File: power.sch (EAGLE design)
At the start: 12 parts, among them IC1 UC27775, J2 USB-MINIB-TH-VERTICAL-5PIN, U1 MCP73831, U2 Tiny85-20-SMT, X1 Micro USB

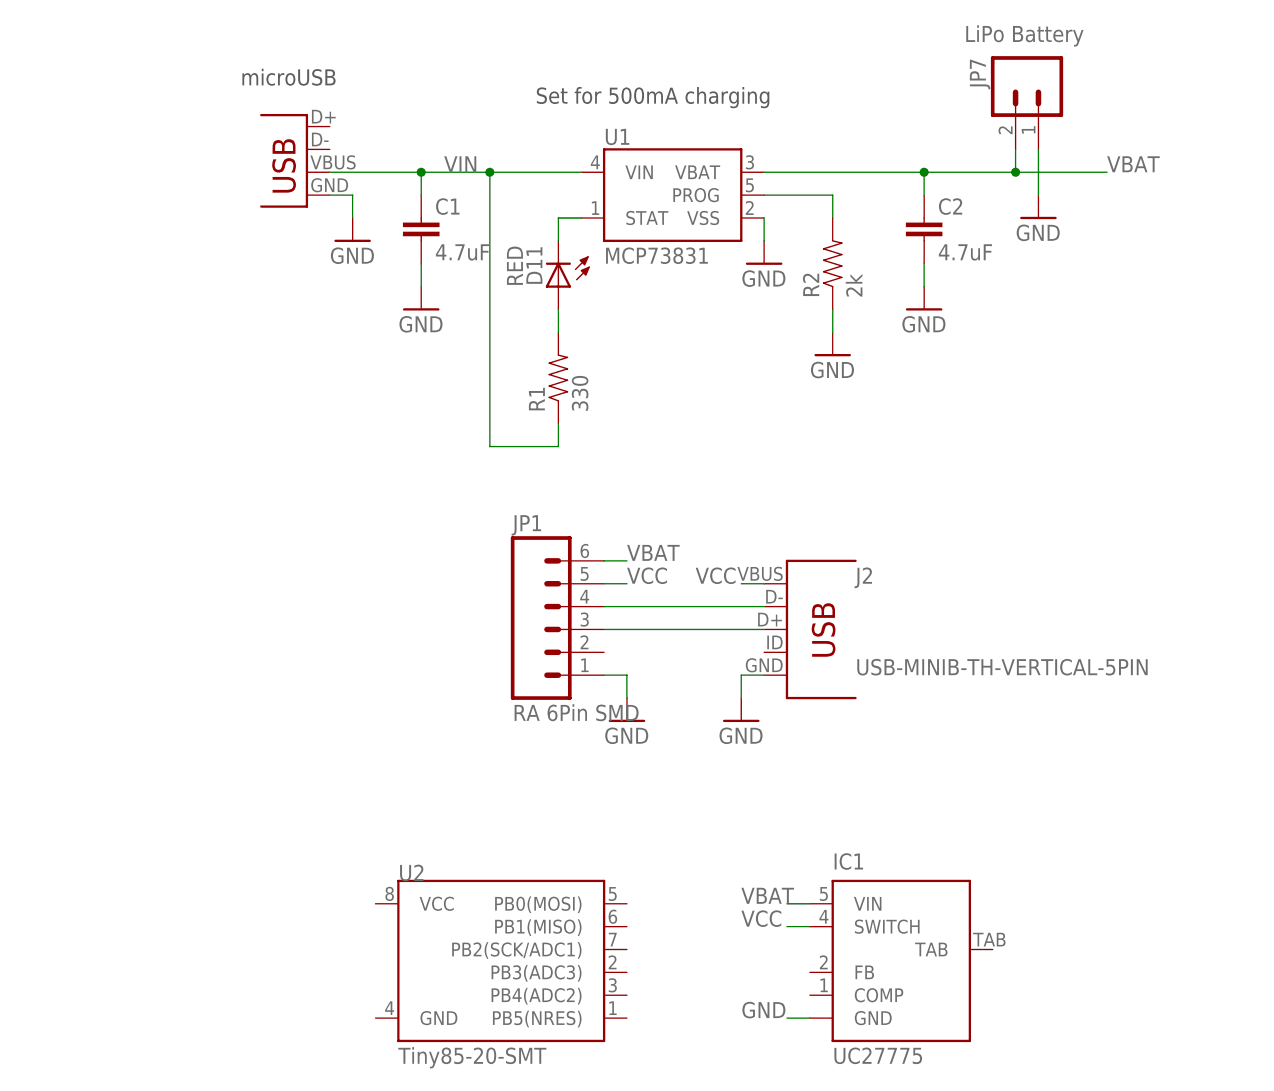
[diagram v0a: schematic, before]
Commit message: Added a switch and cleaned up the drawings
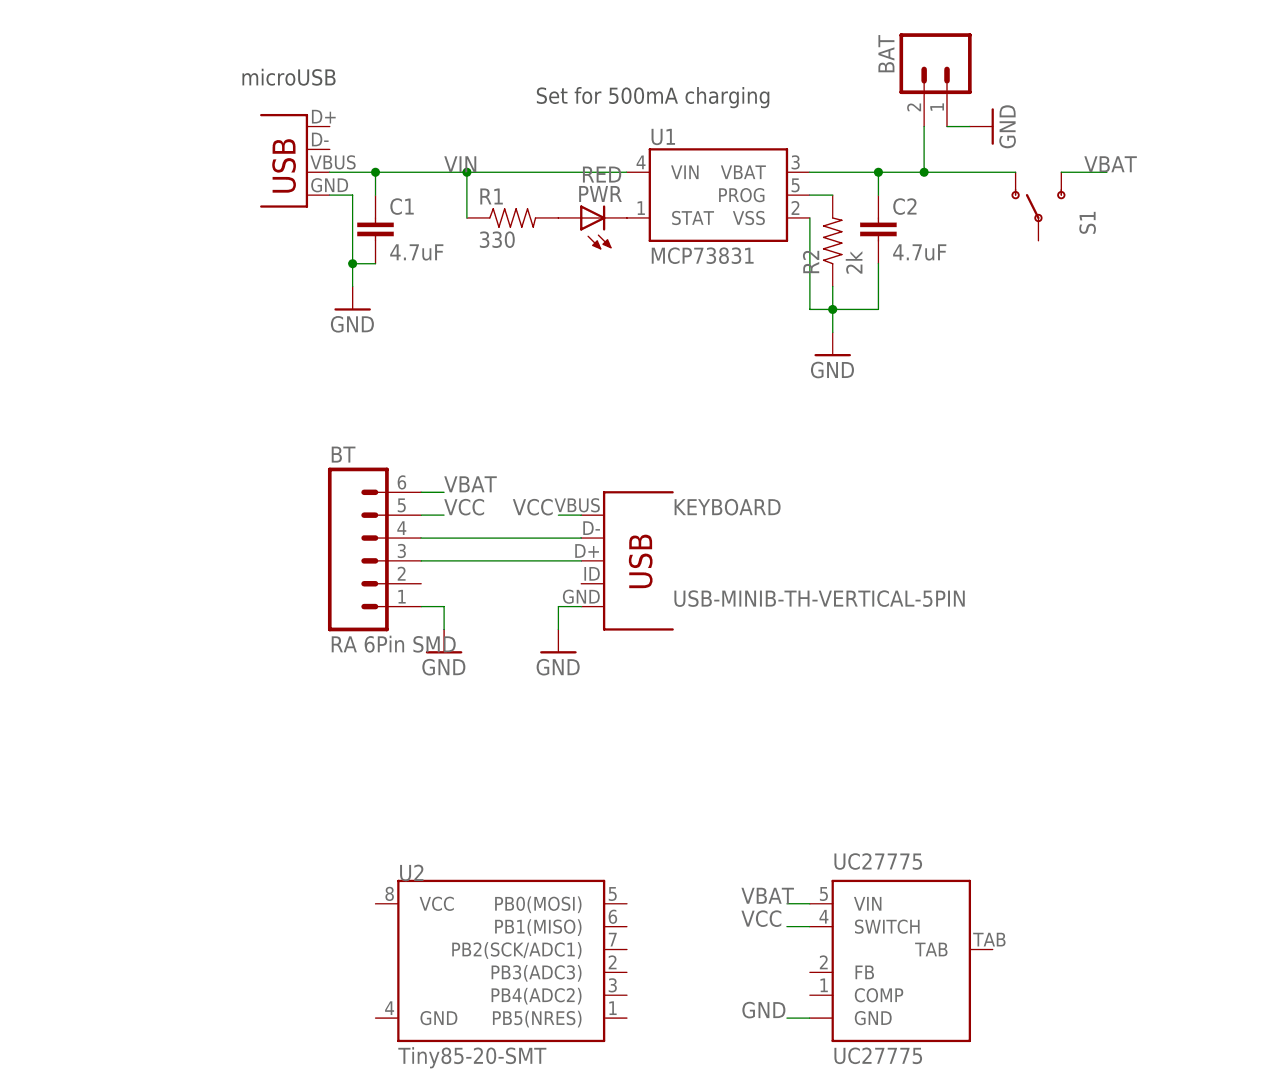
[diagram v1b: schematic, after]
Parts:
- removed D11: RED, SparkFun:LED0603
- removed J2: USB-MINIB-TH-VERTICAL-5PIN, mine:USB-MINIB-TH-VERTICAL-5PIN
- removed JP1: RA 6Pin SMD, mine:M06SMD-NOHOLES
- removed JP7: LiPo Battery, SparkFun:M02-JST-2MM-SMT
- added BAT: LiPo Battery, SparkFun:M02-JST-2MM-SMT
- added BT: RA 6Pin SMD, mine:M06SMD-NOHOLES
- added KEYBOARD: USB-MINIB-TH-VERTICAL-5PIN, mine:USB-MINIB-TH-VERTICAL-5PIN
- added PWR: RED, SparkFun:LED0603
- added S1: (no value), SparkFun-Electromechanical:SWITCH-SPDT-SMD-A
- renumbered IC1 to UC27775
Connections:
- new net VBAT2: BAT.2, C2.1, S1.O, U1.VBAT
- net GND: now also BAT.1, BT.1, KEYBOARD.GND; no longer J2.GND, JP1.1, JP7.1
- net N$12: now also PWR.A; no longer D11.A
- net N$2: now also BT.4, KEYBOARD.D-; no longer J2.D-, JP1.4
- net N$3: now also BT.3, KEYBOARD.D+; no longer J2.D+, JP1.3
- net STAT: now also PWR.C; no longer D11.C
- net VBAT: now also BT.6, S1.S; no longer C2.1, JP1.6, JP7.2, U1.VBAT
- net VCC: now also BT.5, KEYBOARD.VBUS; no longer J2.VBUS, JP1.5
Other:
- moved on the sheet: C1, C2, R1, R2, U1

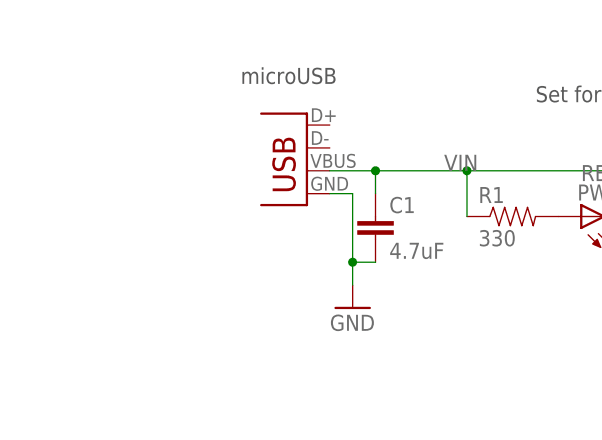
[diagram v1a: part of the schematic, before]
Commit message: Using mini usb instead of micro
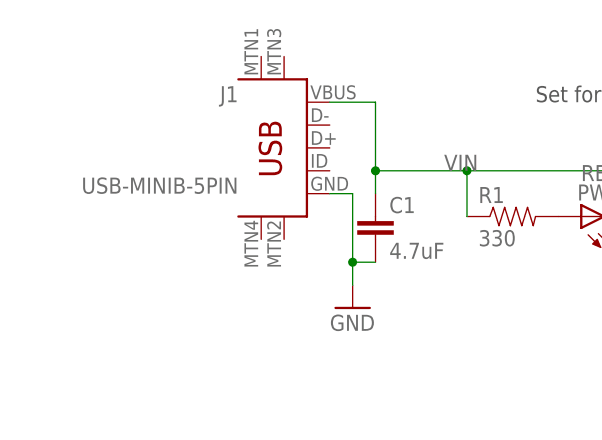
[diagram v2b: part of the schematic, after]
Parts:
- removed X1: Micro USB, SparkFun:USB-MICROB
- added J1: USB-MINIB-5PIN, SparkFun-Connectors:USB-MINIB-5PIN
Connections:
- net GND: now also J1.GND; no longer X1.GND
- net VIN: now also J1.VBUS; no longer X1.VBUS
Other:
- note removed: "microUSB"
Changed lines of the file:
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@@
 <?xml version="1.0" encoding="utf-8"?>
 <!DOCTYPE eagle SYSTEM "eagle.dtd">
-<eagle version="6.6.0">
+<eagle version="7.4.0">
 <drawing>
 <settings>
@@
 <part name="GND19" library="SparkFun" deviceset="GND" device=""/>
 <part name="BAT" library="SparkFun" deviceset="M02" device="-JST-2MM-SMT" value="LiPo Battery"/>
-<part name="X1" library="SparkFun" deviceset="USB" device="-MICROB" value="Micro USB"/>
 <part name="R2" library="SparkFun-Resistors" deviceset="0.22OHM-1/4W-1%(0805)" device="" value="2k"/>
 <part name="C1" library="SparkFun-Capacitors" deviceset="1.0UF-25V-+80/-20(0805)" device="&quot;" value="4.7uF"/>
@@
 <part name="KEYBOARD" library="mine" deviceset="USB-MINIB-TH-VERTICAL" device="-5PIN"/>
 <part name="S1" library="SparkFun-Electromechanical" deviceset="SWITCH-SPDT" device="-SMD-A"/>
+<part name="J1" library="SparkFun-Connectors" deviceset="USB-MINIB" device="-5PIN"/>
 </parts>
 <sheets>
@@
 <plain>
 <text x="167.64" y="142.24" size="1.778" layer="97">Set for 500mA charging</text>
-<text x="134.874" y="144.272" size="1.778" layer="97">microUSB</text>
 </plain>
 <instances>
@@
 <attribute name="NAME" x="207.518" y="149.86" size="1.778" layer="95" rot="MR270"/>
 </instance>
-<instance part="X1" gate="G$1" x="142.24" y="132.08" rot="MR0"/>
 <instance part="R2" gate="G$1" x="200.66" y="127" rot="R90"/>
 <instance part="C1" gate="G$1" x="149.86" y="127"/>
@@
 <instance part="KEYBOARD" gate="G$1" x="175.26" y="86.36"/>
 <instance part="S1" gate="1" x="223.52" y="129.54" rot="R90"/>
+<instance part="J1" gate="G$1" x="142.24" y="132.08" rot="MR0"/>
 </instances>
 <busses>
@@
 <wire x1="147.32" y1="132.08" x2="147.32" y2="124.46" width="0.1524" layer="91"/>
 <pinref part="GND15" gate="1" pin="GND"/>
-<pinref part="X1" gate="G$1" pin="GND"/>
 <wire x1="147.32" y1="124.46" x2="147.32" y2="121.92" width="0.1524" layer="91"/>
 <wire x1="147.32" y1="124.46" x2="149.86" y2="124.46" width="0.1524" layer="91"/>
 <pinref part="C1" gate="G$1" pin="2"/>
 <junction x="147.32" y="124.46"/>
+<pinref part="J1" gate="G$1" pin="GND"/>
 </segment>
 <segment>
@@
 <wire x1="160.02" y1="134.62" x2="177.8" y2="134.62" width="0.1524" layer="91"/>
 <wire x1="160.02" y1="129.54" x2="160.02" y2="134.62" width="0.1524" layer="91"/>
-<wire x1="144.78" y1="134.62" x2="149.86" y2="134.62" width="0.1524" layer="91"/>
 <junction x="149.86" y="134.62"/>
 <junction x="160.02" y="134.62"/>
 <label x="157.48" y="134.62" size="1.778" layer="95"/>
 <pinref part="U1" gate="G$1" pin="VIN"/>
-<pinref part="X1" gate="G$1" pin="VBUS"/>
 <pinref part="C1" gate="G$1" pin="1"/>
 <pinref part="R1" gate="G$1" pin="1"/>
-</segment>
-</net>
+<wire x1="149.86" y1="134.62" x2="149.86" y2="142.24" width="0.1524" layer="91"/>
+<pinref part="J1" gate="G$1" pin="VBUS"/>
+<wire x1="149.86" y1="142.24" x2="144.78" y2="142.24" width="0.1524" layer="91"/>
+</segment>
+</net>
